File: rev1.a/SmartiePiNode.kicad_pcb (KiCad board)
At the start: 2 copper layers, 52 parts, among them CN1 USBMICROb, CN2 ST-LINK, CN3 SX1238_TRX_HEADER, SW1 SW_PUSH, U1 ISL91127IR, U2 STM32L052_LQFP48, X1 abm10, X2 ABS25-32.768KHZ-6-T

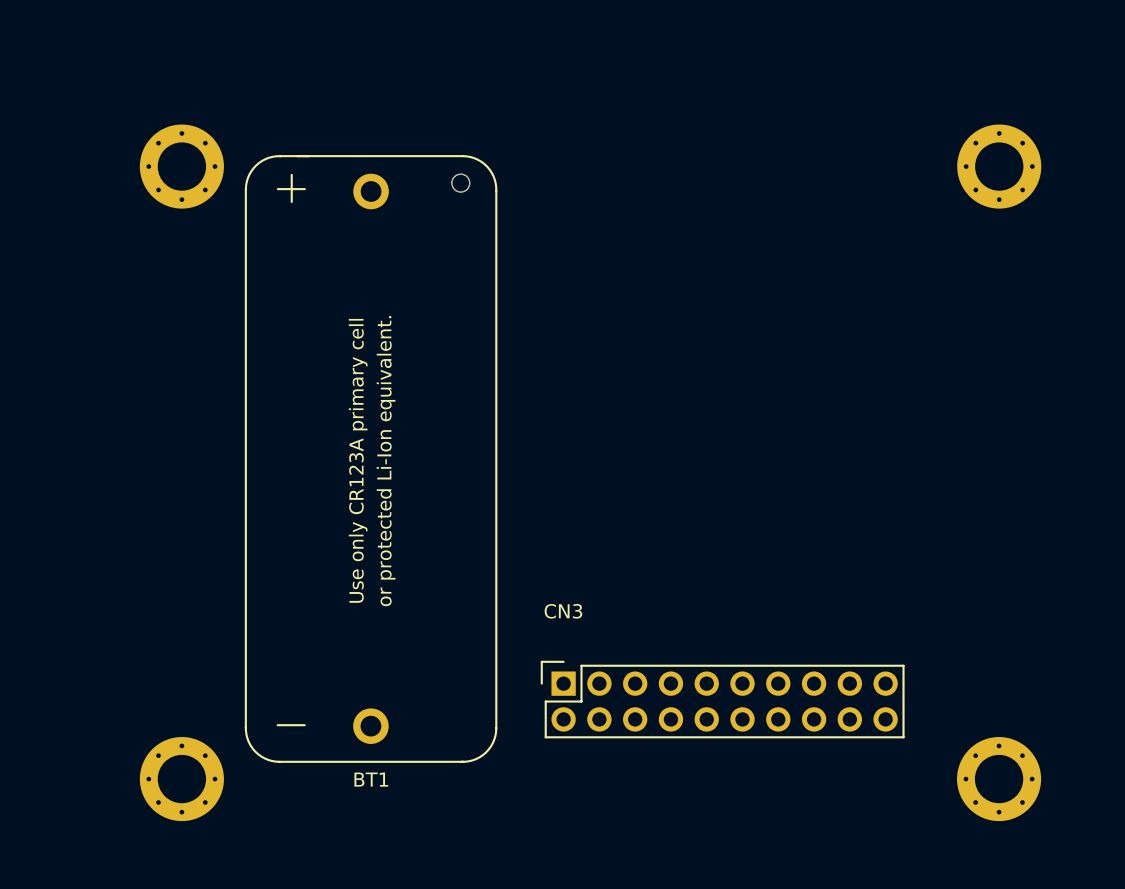
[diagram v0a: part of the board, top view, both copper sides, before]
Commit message: finished board outline with mounting holes
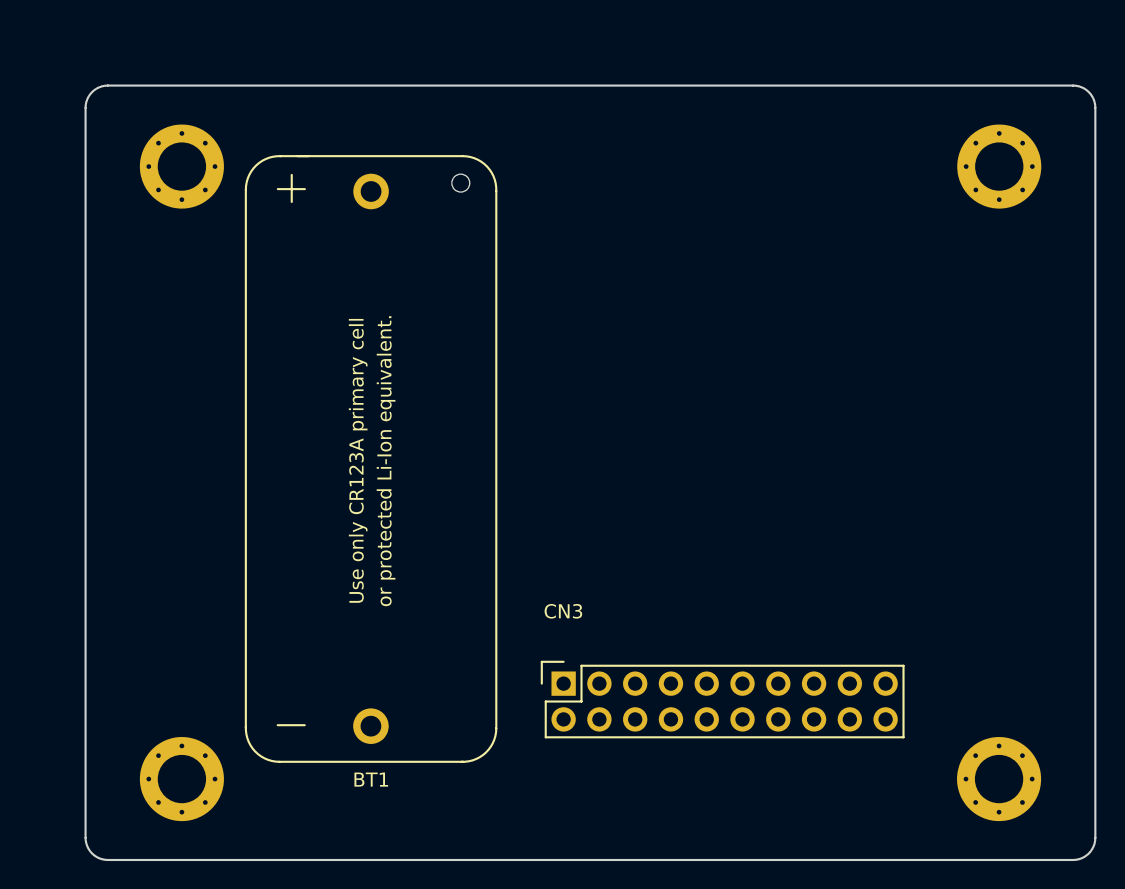
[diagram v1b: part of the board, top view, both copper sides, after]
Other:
- board outline added: 71.7 x 55 mm
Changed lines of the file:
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@@
     (links 156)
     (no_connects 124)
-    (area 0 0 0 0)
+    (area 45.982916 25.735917 179.440001 172.670001)
     (thickness 1.6)
-    (drawings 0)
+    (drawings 12)
     (tracks 0)
     (zones 0)
@@
     (pad_to_mask_clearance 0.2)
     (aux_axis_origin 0 0)
-    (visible_elements FFFFFF7F)
+    (visible_elements 7FFFFFFF)
     (pcbplotparams
       (layerselection 0x00030_ffffffff)
@@
       (effects (font (size 1 1) (thickness 0.15)))
     )
-    (fp_text value m3-mounting-hole (at -0.02 -4.19) (layer F.Fab) hide
+    (fp_text value m3-mounting-hole (at 2.12 -3.85) (layer F.Fab) hide
       (effects (font (size 1 1) (thickness 0.15)))
     )
@@
       (effects (font (size 1 1) (thickness 0.15)))
     )
-    (fp_text value m3-mounting-hole (at -0.02 -4.19) (layer F.Fab) hide
+    (fp_text value m3-mounting-hole (at -2.627189 -4.29) (layer F.Fab) hide
       (effects (font (size 1 1) (thickness 0.15)))
     )
@@
       (net 1 GND))
   )
+  (gr_line (start 106.06 117.99) (end 106.06 117.99) (layer Edge.Cuts) (width 0.15))
+  (gr_line (start 106.06 169.8) (end 106.06 117.99) (layer Edge.Cuts) (width 0.15))
+  (gr_line (start 107.65 171.38) (end 107.65 171.38) (layer Edge.Cuts) (width 0.15))
+  (gr_line (start 176.17 171.38) (end 107.65 171.38) (layer Edge.Cuts) (width 0.15))
+  (gr_line (start 177.75 169.8) (end 177.75 169.8) (layer Edge.Cuts) (width 0.15))
+  (gr_line (start 177.75 117.98) (end 177.75 169.8) (layer Edge.Cuts) (width 0.15))
+  (gr_line (start 176.16 116.4) (end 176.16 116.4) (layer Edge.Cuts) (width 0.15))
+  (gr_line (start 107.64 116.4) (end 176.16 116.4) (layer Edge.Cuts) (width 0.15))
+  (gr_arc (start 176.17 169.8) (end 177.75 169.8) (angle 90) (layer Edge.Cuts) (width 0.15))
+  (gr_arc (start 176.17 117.98) (end 176.17 116.4) (angle 90) (layer Edge.Cuts) (width 0.15))
+  (gr_arc (start 107.64 117.98) (end 106.06 117.98) (angle 90) (layer Edge.Cuts) (width 0.15))
+  (gr_arc (start 107.64 169.8) (end 107.64 171.38) (angle 90) (layer Edge.Cuts) (width 0.15))
 )

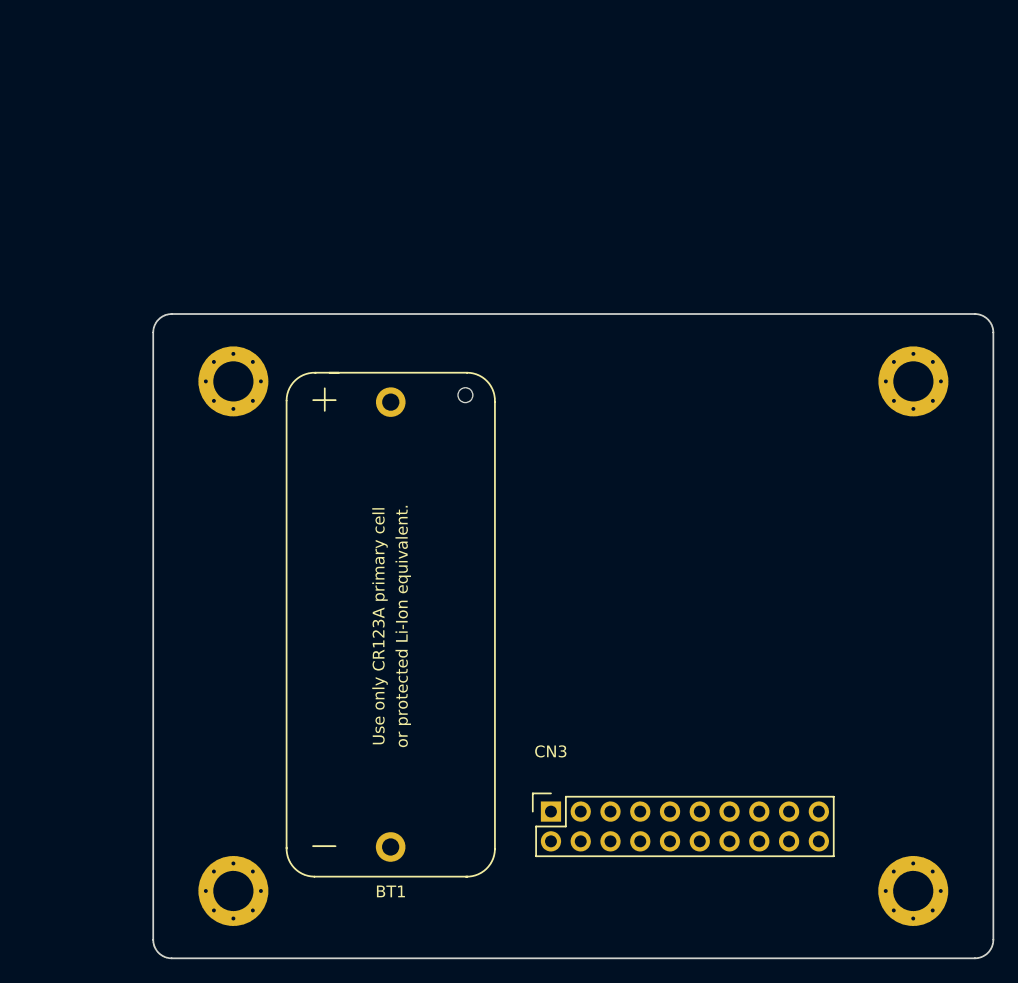
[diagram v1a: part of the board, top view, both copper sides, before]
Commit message: footprint for sx1238 trx module
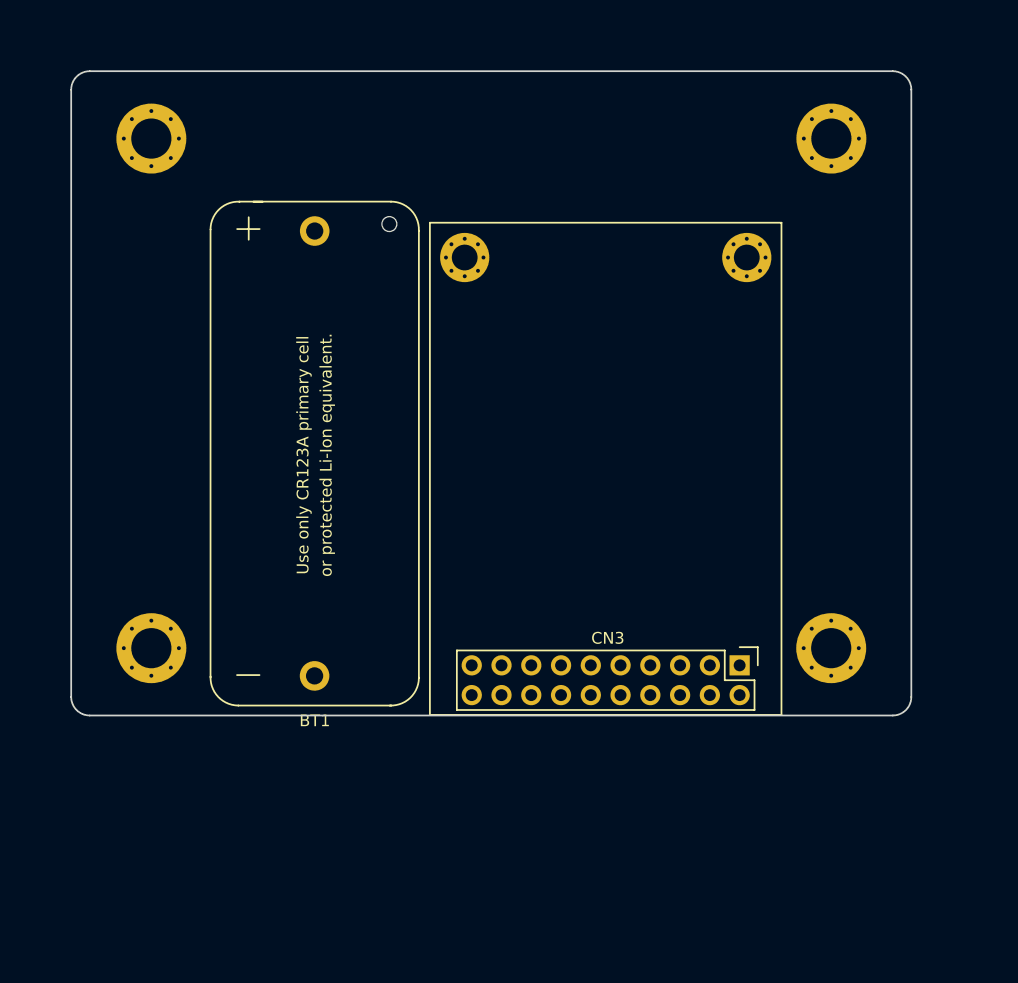
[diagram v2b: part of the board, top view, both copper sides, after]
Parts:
- CN3: footprint Socket_Strips:Socket_Strip_Straight_2x10 -> socket-strip-straight-2x10:sx1238_trx
- moved H1 21.9 mm to (105.9, 144.9)
- moved H2 21.9 mm to (105.9, 101.4)
- moved H3 21.9 mm to (163.9, 144.9)
- moved H4 21.9 mm to (163.9, 101.4)
- moved CN3 20.4 mm to (156.1, 146.4), turned to 270 degrees
- moved BT1 16.0 mm to (119.8, 128.3)

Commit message: starting pcb components placement
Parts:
- moved C13 123.4 mm to (174.0, 136.1)
- moved CN1 114.0 mm to (167.9, 122.4), turned to 90 degrees
- moved U2 110.3 mm to (150.1, 123.7)
- moved C14 105.7 mm to (153.4, 129.8), turned to 180 degrees
- moved C5 105.1 mm to (180.0, 68.2), turned to 270 degrees
- moved X2 104.7 mm to (136.9, 117.8), turned to 90 degrees
- moved R2 104.6 mm to (161.2, 123.7)
- moved C17 102.8 mm to (156.2, 120.7), turned to 270 degrees
- moved C7 101.6 mm to (165.3, 68.5), turned to 270 degrees
- moved X1 96.3 mm to (137.2, 126.7), turned to 180 degrees
- moved U1 96.2 mm to (155.6, 68.2), turned to 270 degrees
- moved R3 95.6 mm to (161.2, 122.0)
- moved L1 95.4 mm to (155.7, 57.5)
- moved C8 95.1 mm to (175.0, 68.3), turned to 270 degrees
- moved R9 95.1 mm to (151.1, 116.1)
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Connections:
- X2 pad 2: (no net) -> Net-(C18-Pad2)

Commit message: more pcb layout/parts placement.
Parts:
- moved CN2 136.1 mm to (169.0, 127.7)
- moved C16 127.9 mm to (185.2, 123.1)
- moved C15 117.8 mm to (179.1, 125.0)
- moved D2 83.0 mm to (131.4, 147.4), turned to 90 degrees
- moved F1 82.4 mm to (157.4, 138.5), turned to 180 degrees
- moved C1 72.0 mm to (157.5, 136.4), turned to 0 degrees
- moved L1 71.5 mm to (152.9, 128.9), turned to 90 degrees
- moved C2 69.4 mm to (157.5, 134.5), turned to 0 degrees
- moved D1 68.1 mm to (166.8, 121.8), turned to 90 degrees
- moved C4 67.4 mm to (157.5, 132.8), turned to 0 degrees
- moved R4 62.2 mm to (163.7, 135.1), turned to 0 degrees
- moved C5 61.0 mm to (163.4, 126.9)
- moved U1 60.8 mm to (157.6, 129.0), turned to 0 degrees
- moved R6 60.8 mm to (161.7, 126.9), turned to 270 degrees
- moved R5 60.0 mm to (163.7, 133.2)
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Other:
- rule pad_to_mask_clearance: 0.2 -> 0.0762

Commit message: more placement and layout.
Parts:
- moved C10 12.1 mm to (137.7, 117.2)
- moved X1 11.6 mm to (137.8, 115.1)
- moved C11 11.3 mm to (137.8, 112.9)
- moved C19 10.9 mm to (136.4, 108.6), turned to 270 degrees
- moved X2 7.97 mm to (138.3, 110.0)
- moved C18 7.90 mm to (138.9, 107.1), turned to 180 degrees
- moved R13 2.02 mm to (140.9, 109.5)
- moved L1 1.71 mm to (154.5, 129.5)
- moved R14 1.60 mm to (141.0, 111.4)
- moved U1 1.22 mm to (158.7, 129.5)
- moved C1 1.22 mm to (158.6, 136.9)
- moved C4 1.22 mm to (158.6, 133.3)
- moved C7 1.22 mm to (158.7, 123.9)
- moved C8 1.22 mm to (158.7, 122.3)
- moved R6 1.22 mm to (162.8, 127.4)
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
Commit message: more layout
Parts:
- added R15: 10K, Resistors_SMD:R_0603, F.Cu at (163.3, 136.1)
- R4: value 0 -> 10K
- moved C16 42.4 mm to (145.2, 109.1), turned to 90 degrees
- moved C15 38.2 mm to (143.6, 110.8), turned to 90 degrees
- moved C19 1.91 mm to (136.7, 110.5)
- moved C18 1.63 mm to (139.0, 108.8)
- moved R13 1.58 mm to (141.1, 111.1)
- moved R14 1.58 mm to (141.1, 113.0)
- moved X2 1.58 mm to (138.4, 111.6)
- moved C10 1.48 mm to (137.9, 118.7)
- moved C11 1.48 mm to (138.0, 114.3)
- moved R11 1.48 mm to (141.3, 115.8)
- moved X1 1.48 mm to (138.0, 116.6)
- moved R12 1.48 mm to (141.3, 117.4)
- moved R10 0.85 mm to (147.7, 109.2)
- moved R9 0.78 mm to (149.3, 109.1)
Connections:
- U1 pad 11: /+VIN -> Net-(R15-Pad1)

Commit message: more layout
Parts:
- moved C9 114.6 mm to (165.8, 121.3), turned to 90 degrees
- moved SW1 111.6 mm to (163.1, 124.2), turned to 90 degrees
- moved R8 102.9 mm to (158.8, 120.7), turned to 180 degrees
- moved C13 35.0 mm to (143.2, 123.2)
- moved D1 1.98 mm to (168.8, 121.8)
- moved L2 1.07 mm to (143.2, 120.3), turned to 0 degrees
- moved C12 1.04 mm to (143.2, 121.6), turned to 0 degrees

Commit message: tweaking final layout a bit more.
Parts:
- moved C19 3.00 mm to (136.8, 113.5)
- moved C16 2.81 mm to (144.8, 111.8)
- moved CN2 2.12 mm to (168.8, 129.8)
- moved CN1 1.57 mm to (167.2, 115.3)
- moved R9 1.52 mm to (148.6, 110.5), turned to 0 degrees
- moved C12 1.44 mm to (143.3, 123.0)
- moved C17 1.44 mm to (153.2, 112.1)
- moved C18 1.44 mm to (139.1, 110.2)
- moved R12 1.44 mm to (141.4, 118.8)
- moved R2 1.44 mm to (155.9, 116.8)
- moved X2 1.44 mm to (138.6, 113.0)
- moved R13 1.44 mm to (141.2, 112.5)
- moved C10 1.44 mm to (138.1, 120.1)
- moved C11 1.44 mm to (138.1, 115.8)
- moved C13 1.44 mm to (143.3, 124.6)
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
